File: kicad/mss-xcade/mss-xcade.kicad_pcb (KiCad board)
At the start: 2 copper layers, 133.4 x 127 mm, 233 parts, among them J1 Screw_Terminal_01x02, J10 8P8C, J11 Molex 0532610471, J12 Molex 0532610471, J13 Molex 0532610471, J14 Molex 0532610471, J15 Screw_Terminal_01x02, J16 Screw_Terminal_01x02, J17 Screw_Terminal_01x02, J18 Screw_Terminal_01x02, J19 Screw_Terminal_01x02, J2 SM04B-SRSS, J21 Screw_Terminal_01x02, J23 Screw_Terminal_01x02, J24 Screw_Terminal_01x02, J25 Screw_Terminal_01x02, J26 Screw_Terminal_01x02, J27 Molex 0532610471, J28 Molex 0532610471, J29 Molex 0532610471, J3 690-005-299-043, J30 Molex 0532610471, J31 AVR-ISP, J32 SM04B-SRSS, J33 SM04B-SRSS, J34 SM04B-SRSS, J35 SM04B-SRSS, J36 SM04B-SRSS, J37 SM04B-SRSS, J38 SM04B-SRSS, J39 SM04B-SRSS, J4 SM04B-SRSS, J40 SM04B-SRSS, J41 SM04B-SRSS, J42 Screw_Terminal_01x08, J5 Conn_02x03_Odd_Even, J6 SM04B-SRSS, J7 8P8C, J8 8P8C, J9 8P8C, Q1 ZXMS6004FF, Q10 ZXMS6004FF, Q11 ZXMS6004FF, Q12 ZXMS6004FF, Q13 ZXMS6004FF, Q14 ZXMS6004FF, Q15 ZXMS6004FF, Q16 ZXMS6004FF, Q2 ZXMS6004FF, Q3 ZXMS6004FF, Q4 ZXMS6004FF, Q5 ZXMS6004FF, Q6 ZXMS6004FF, Q7 ZXMS6004FF, Q8 ZXMS6004FF, Q9 ZXMS6004FF, SW1 FSM4JSMATR, SW2 SW_DIP_x08, SW3 JS202011SCQN, U1 AZ1117-3.3, U10 74HC4049, U11 TCA9555PWR, U12 ATtiny88-A, U13 TCA9555PWR, U2 AP63205WU, U3 PCA9546ADR, U4 ESP32-S2-SOLO, U5 AP3012, U6 74HC4049, U7 74HC4049, U8 TCA9555PWR, U9 74HC4049

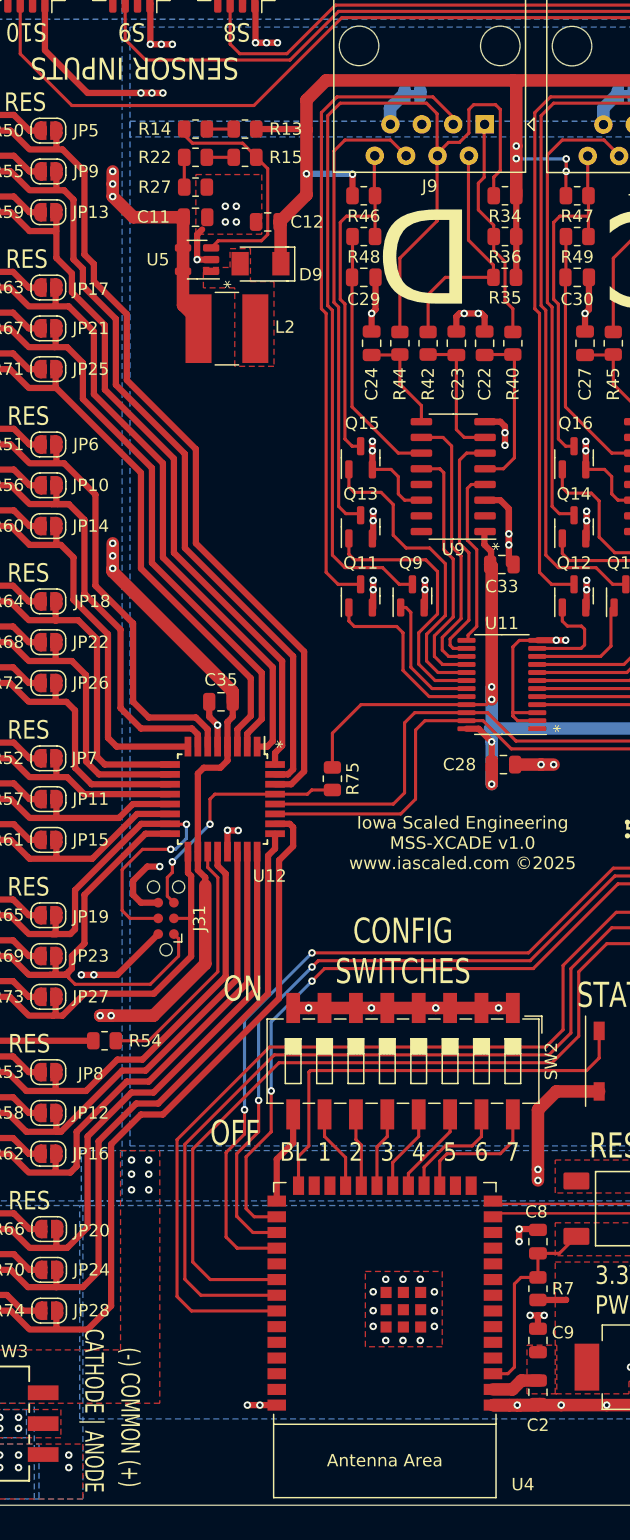
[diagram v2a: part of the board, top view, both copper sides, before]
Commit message: Fix anode/cathode text, update version number
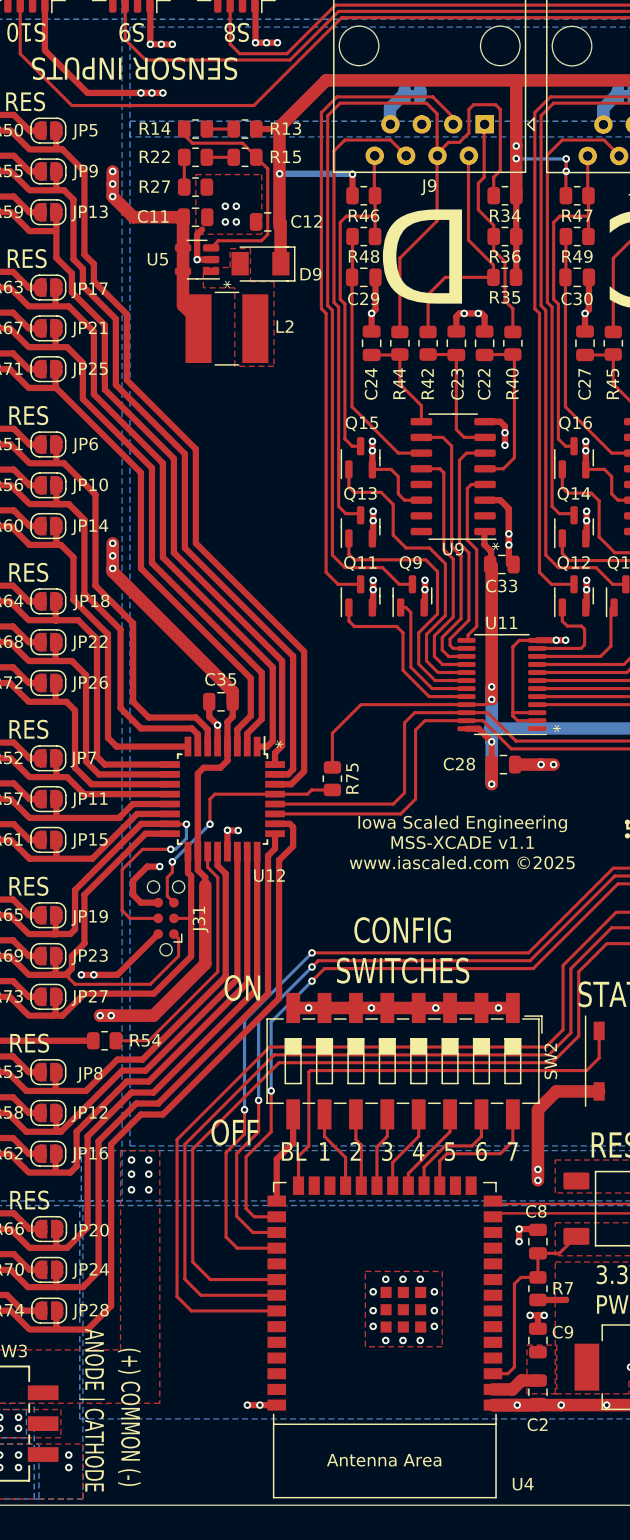
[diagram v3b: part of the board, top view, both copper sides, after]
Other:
- board text added: "(+) COMMON (-)"
- board text added: "ANODE | CATHODE"
- board text added: "Iowa Scaled Engineering MSS-XCADE v1.1 www.iascaled.com ©2025"
- board text removed: "(-) COMMON (+)"
- board text removed: "CATHODE | ANODE"
- board text removed: "Iowa Scaled Engineering MSS-XCADE v1.0 www.iascaled.com ©2025"
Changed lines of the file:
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@@
     (effects (font (size 1.5 1.27) (thickness 0.3)))
   )
-  (gr_text " CATHODE | ANODE" (at 112.649 141.986 270) (layer "F.SilkS")
+  (gr_text " ANODE | CATHODE" (at 112.649 141.986 270) (layer "F.SilkS")
     (effects (font (size 1.5 1.016) (thickness 0.254)))
   )
@@
     (effects (font (size 2.032 1.524) (thickness 0.3)))
   )
-  (gr_text "Iowa Scaled Engineering\nMSS-XCADE v1.0\nwww.iascaled.com ©2025" (at 142.494 96.266) (layer "F.SilkS")
+  (gr_text "Iowa Scaled Engineering\nMSS-XCADE v1.1\nwww.iascaled.com ©2025" (at 142.494 96.266) (layer "F.SilkS")
     (effects (font (size 1.016 1.016) (thickness 0.1524)))
   )
@@
     (effects (font (size 1 1) (thickness 0.15)))
   )
-  (gr_text "(-) COMMON (+)" (at 115.57 142.748 270) (layer "F.SilkS")
+  (gr_text "(+) COMMON (-)" (at 115.57 142.748 270) (layer "F.SilkS")
     (effects (font (size 1.5 1.016) (thickness 0.254)))
   )
@@
   (segment (start 181.1255 43.8785) (end 181.1255 34.5675) (width 1.016) (layer "F.Cu") (net 15))
   (segment (start 197.231 34.798) (end 196.977 34.544) (width 1.016) (layer "F.Cu") (net 15))
-  (segment (start 131.445 34.544) (end 146.558 34.544) (width 1.016) (layer "F.Cu") (net 15))
+  (segment (start 125.79325 38.481) (end 127.6858 38.481) (width 0.508) (layer "F.Cu") (net 15))
   (segment (start 164.1075 43.8785) (end 164.1075 50.459) (width 0.508) (layer "F.Cu") (net 15))
   (segment (start 181.1255 50.459) (end 181.102 50.4825) (width 0.508) (layer "F.Cu") (net 15))
   (segment (start 146.8355 43.8785) (end 146.8355 50.459) (width 0.508) (layer "F.Cu") (net 15))
-  (segment (start 129.855 43.81365) (end 129.855 38.542) (width 1.016) (layer "F.Cu") (net 15))
   (segment (start 146.8355 39.8545) (end 146.8355 34.8215) (width 1.016) (layer "F.Cu") (net 15))
-  (segment (start 129.855 36.134) (end 131.445 34.544) (width 1.016) (layer "F.Cu") (net 15))
-  (segment (start 129.794 38.481) (end 129.855 38.542) (width 0.508) (layer "F.Cu") (net 15))
+  (segment (start 131.445 34.544) (end 146.558 34.544) (width 1.016) (layer "F.Cu") (net 15))
   (segment (start 146.8355 43.8785) (end 146.8355 40.8705) (width 1.016) (layer "F.Cu") (net 15))
-  (segment (start 125.79325 38.481) (end 129.794 38.481) (width 0.508) (layer "F.Cu") (net 15))
+  (segment (start 127.66925 38.31975) (end 131.445 34.544) (width 1.016) (layer "F.Cu") (net 15))
   (segment (start 164.1075 34.5675) (end 164.084 34.544) (width 1.016) (layer "F.Cu") (net 15))
   (segment (start 181.1255 43.8785) (end 181.1255 50.459) (width 0.508) (layer "F.Cu") (net 15))
@@
   (segment (start 181.1255 34.5675) (end 181.102 34.544) (width 1.016) (layer "F.Cu") (net 15))
   (segment (start 127.76 46.09015) (end 127.66925 45.9994) (width 1.016) (layer "F.Cu") (net 15))
-  (segment (start 129.855 38.542) (end 129.855 36.134) (width 1.016) (layer "F.Cu") (net 15))
   (segment (start 167.894 43.601) (end 167.894 41.91) (width 0.254) (layer "F.Cu") (net 15))
   (segment (start 198.1435 43.942) (end 198.1435 50.5225) (width 0.508) (layer "F.Cu") (net 15))
@@
   (segment (start 146.8355 40.8705) (end 146.8355 39.8545) (width 1.016) (layer "F.Cu") (net 15))
   (segment (start 198.1435 50.5225) (end 198.12 50.546) (width 0.508) (layer "F.Cu") (net 15))
+  (segment (start 127.66925 45.9994) (end 127.66925 38.31975) (width 1.016) (layer "F.Cu") (net 15))
   (segment (start 150.8525 43.8785) (end 150.8525 41.9335) (width 0.254) (layer "F.Cu") (net 15))
   (segment (start 184.912 41.91) (end 184.912 40.894) (width 0.254) (layer "F.Cu") (net 15))
@@
   (segment (start 150.8525 41.9335) (end 150.876 41.91) (width 0.254) (layer "F.Cu") (net 15))
   (segment (start 164.084 34.544) (end 146.558 34.544) (width 1.016) (layer "F.Cu") (net 15))
-  (segment (start 127.66925 45.9994) (end 129.855 43.81365) (width 1.016) (layer "F.Cu") (net 15))
   (via (at 167.894 41.91) (size 0.6096) (drill 0.3048) (layers "F.Cu" "B.Cu") (net 15))
   (via (at 184.912 40.894) (size 0.6096) (drill 0.3048) (layers "F.Cu" "B.Cu") (net 15))
@@
   (via (at 150.876 41.91) (size 0.6096) (drill 0.3048) (layers "F.Cu" "B.Cu") (net 15))
   (via (at 184.912 41.91) (size 0.6096) (drill 0.3048) (layers "F.Cu" "B.Cu") (net 15))
-  (via (at 129.855 42.103) (size 0.6096) (drill 0.3048) (layers "F.Cu" "B.Cu") (net 15))
+  (via (at 127.6858 42.103) (size 0.6096) (drill 0.3048) (layers "F.Cu" "B.Cu") (net 15))
   (via (at 181.102 39.878) (size 0.6096) (drill 0.3048) (layers "F.Cu" "B.Cu") (net 15))
   (via (at 167.894 40.894) (size 0.6096) (drill 0.3048) (layers "F.Cu" "B.Cu") (net 15))
@@
   (segment (start 146.8355 39.8545) (end 146.8355 40.8705) (width 0.254) (layer "B.Cu") (net 15))
   (segment (start 184.912 41.91) (end 184.912 40.894) (width 0.254) (layer "B.Cu") (net 15))
+  (segment (start 133.543 42.103) (end 133.5805 42.1405) (width 0.508) (layer "B.Cu") (net 15))
   (segment (start 167.9175 40.8705) (end 164.1545 40.8705) (width 0.254) (layer "B.Cu") (net 15))
   (segment (start 164.131 39.831) (end 164.131 40.847) (width 0.254) (layer "B.Cu") (net 15))
@@
   (segment (start 184.8885 40.9175) (end 181.1255 40.9175) (width 0.254) (layer "B.Cu") (net 15))
   (segment (start 184.912 40.894) (end 184.8885 40.9175) (width 0.254) (layer "B.Cu") (net 15))
-  (segment (start 133.543 42.103) (end 129.855 42.103) (width 0.508) (layer "B.Cu") (net 15))
-  (segment (start 133.5805 42.1405) (end 133.543 42.103) (width 0.508) (layer "B.Cu") (net 15))
+  (segment (start 127.6858 42.103) (end 133.543 42.103) (width 0.508) (layer "B.Cu") (net 15))
   (segment (start 176.276 62.8015) (end 176.276 56.7665) (width 0.254) (layer "F.Cu") (net 16))
   (segment (start 178.597 63.4365) (end 176.911 63.4365) (width 0.254) (layer "F.Cu") (net 16))
@@
   )
   (zone (net 2) (net_name "GND") (layer "B.Cu") (hatch edge 0.508)
-    (connect_pads yes (clearance 0.254))
+    (connect_pads (clearance 0.254))
     (min_thickness 0.254) (filled_areas_thickness no)
     (fill yes (thermal_gap 0.508) (thermal_bridge_width 0.508))
